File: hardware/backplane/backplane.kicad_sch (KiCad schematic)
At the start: 0 parts

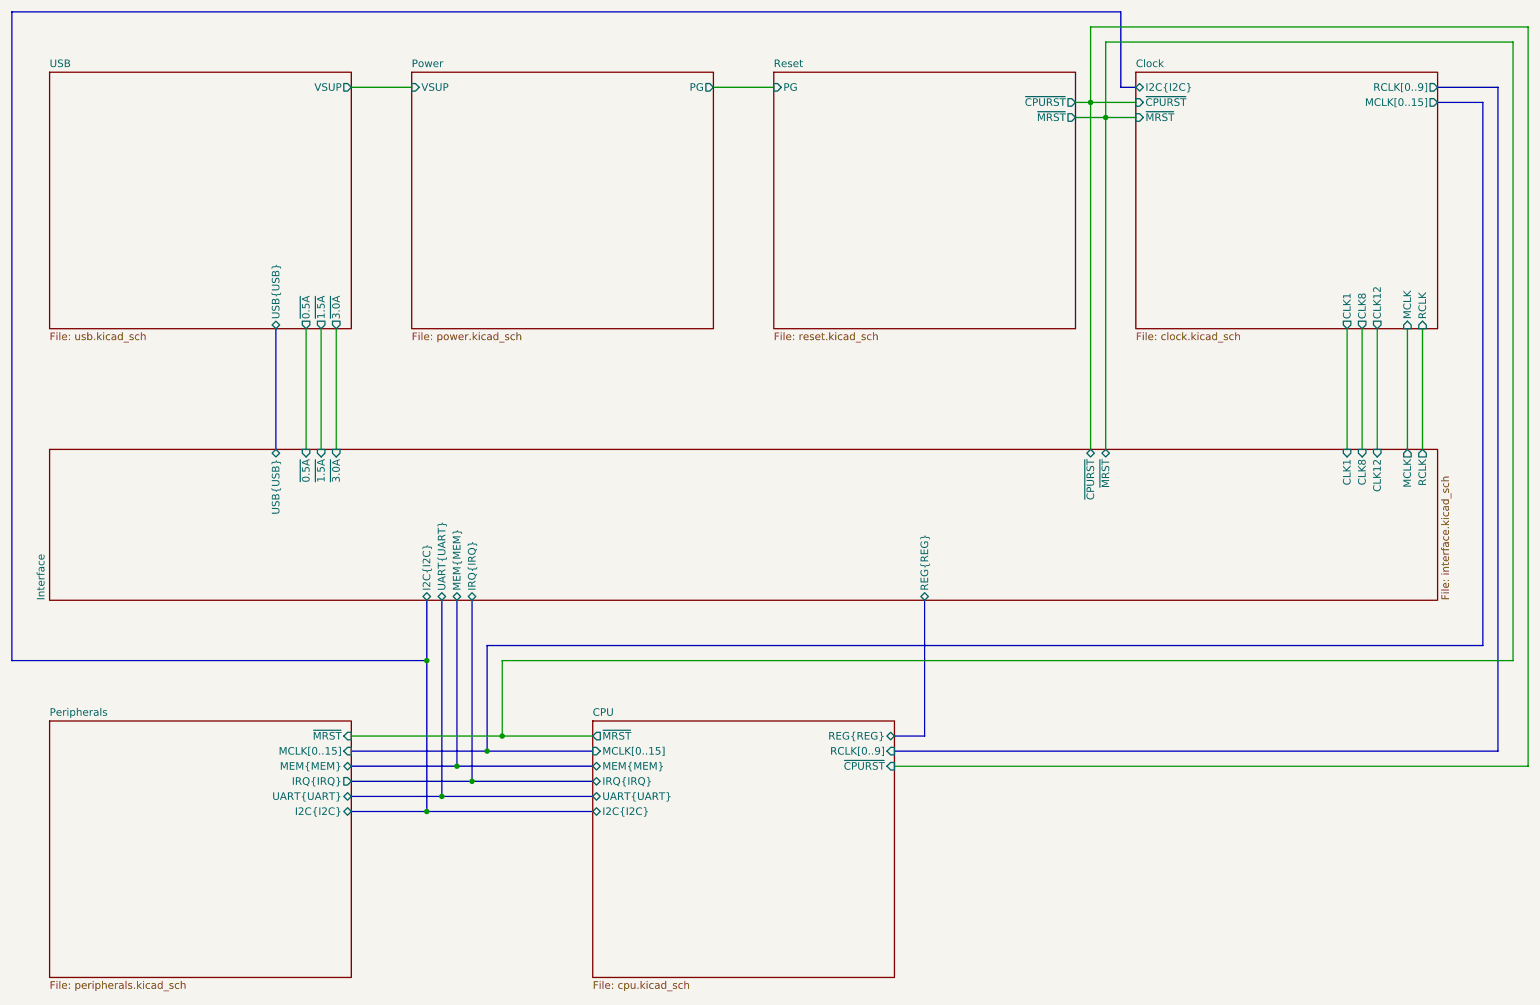
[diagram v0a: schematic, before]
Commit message: feat: Re-add peripheral MCLK, add to memory lines (#3)
Need MCLK to maintain peripheral synchronization.  Add missing memory
access size and latch lines.
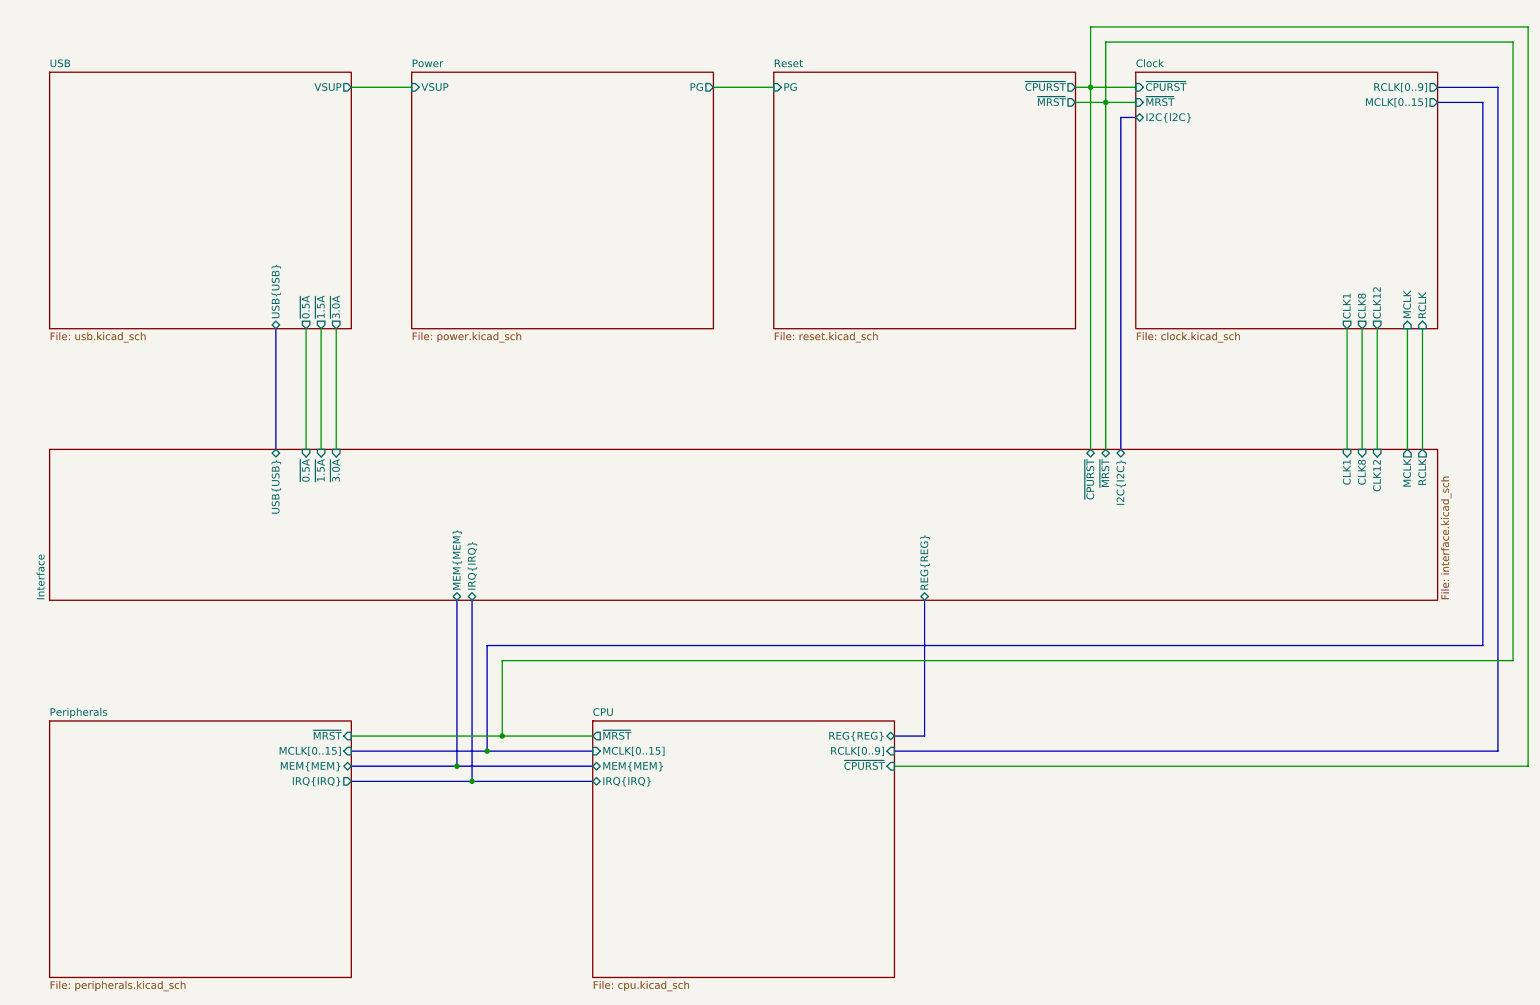
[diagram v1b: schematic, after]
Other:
- sheet CPU ports: added none; removed I2C{I2C}, UART{UART}
- sheet Interface ports: added none; removed UART{UART}
- sheet Peripherals ports: added none; removed I2C{I2C}, UART{UART}

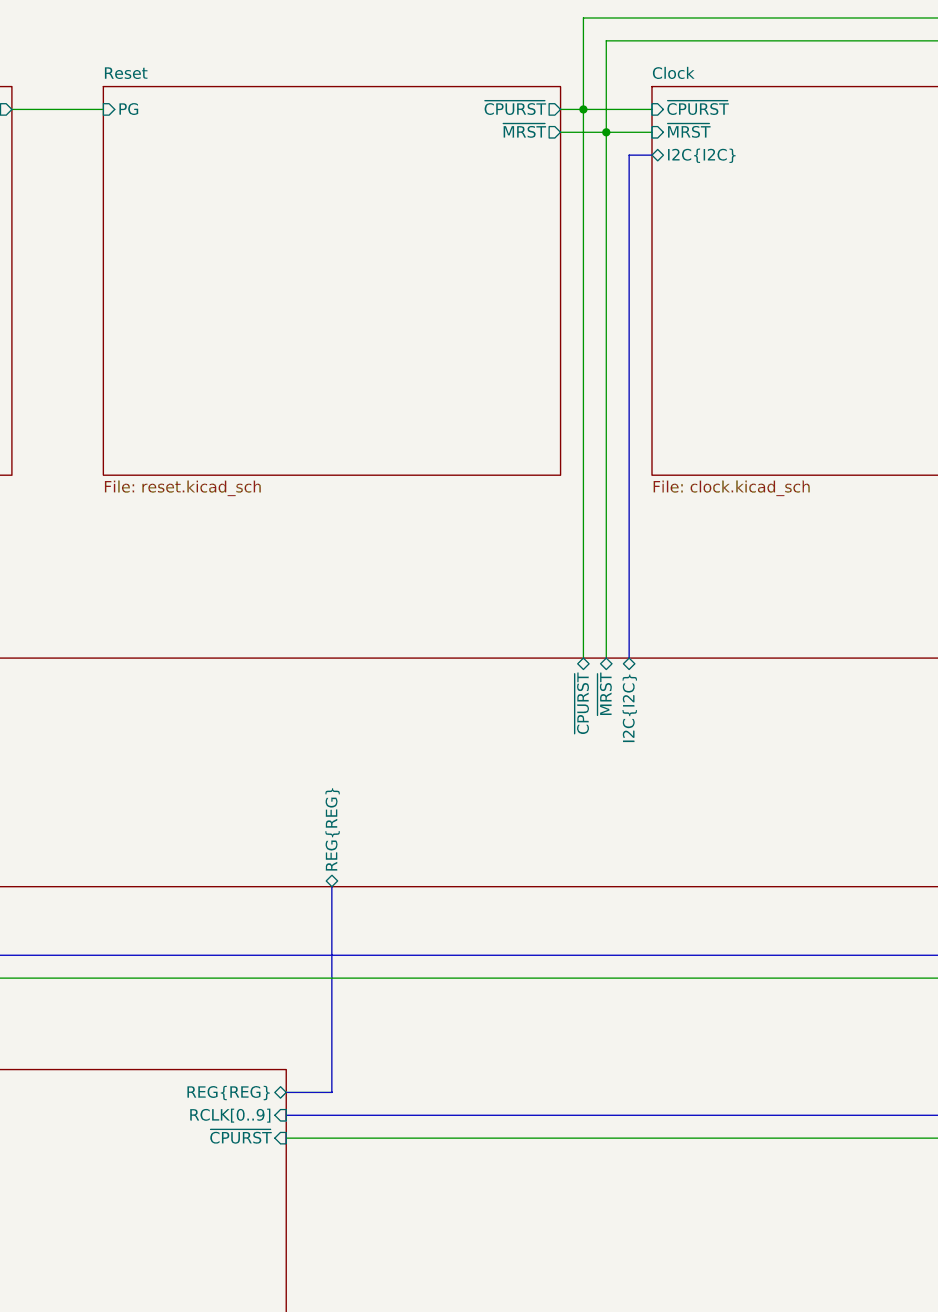
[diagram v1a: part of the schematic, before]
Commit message: feat: Apply bus arch changes to backplane schematic
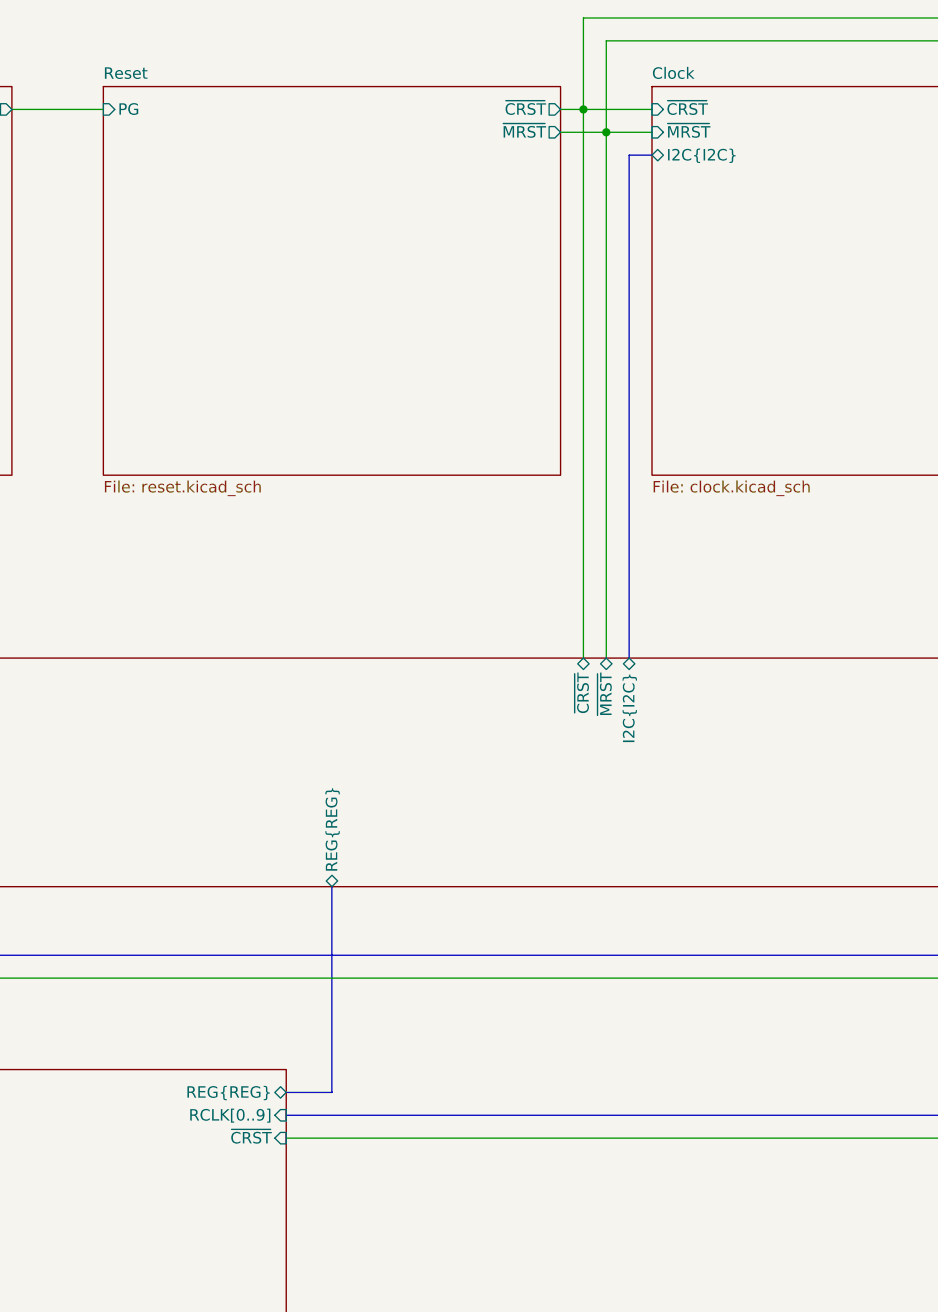
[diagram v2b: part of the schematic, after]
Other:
- sheet CPU ports: added ~{CRST}; removed ~{CPURST}
- sheet Clock ports: added ~{CRST}; removed ~{CPURST}
- sheet Interface ports: added ~{CRST}; removed ~{CPURST}
- sheet Reset ports: added ~{CRST}; removed ~{CPURST}
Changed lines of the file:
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@@
 	)
 	(bus_alias "MEM"
-		(members "A[0..27]" "D[0..31]" "RE" "WE" "HALFWORD" "BYTE" "LATCH")
+		(members "A[0..27]" "D[0..31]" "HALF[0..1]" "~{ARDY}" "~{DRDY}" "~{FAULT}"
+			"~{WR}"
+		)
 	)
 	(bus_alias "REG"
-		(members "SEL[0..11]" "D[0..31]" "DIR")
-	)
-	(bus_alias "SID"
-		(members "[0..3]")
+		(members "R[0..11]" "D[0..31]" "~{WR}")
 	)
 	(bus_alias "UART"
@@
 			)
 		)
-		(pin "~{CPURST}" input
+		(pin "~{CRST}" input
 			(at 165.1 146.05 0)
 			(effects
@@
 			)
 		)
-		(pin "~{CPURST}" bidirectional
+		(pin "~{CRST}" bidirectional
 			(at 198.12 92.71 90)
 			(effects
@@
 			)
 		)
-		(pin "~{CPURST}" input
+		(pin "~{CRST}" input
 			(at 205.74 31.75 180)
 			(effects
@@
 			)
 		)
+		(pin "~{CRST}" output
+			(at 195.58 31.75 0)
+			(effects
+				(font
+					(size 1.27 1.27)
+				)
+				(justify right)
+			)
+		)
 		(pin "~{MRST}" output
 			(at 195.58 34.29 0)
 			(effects
 				(font
-					(size 1.27 1.27)
-				)
-				(justify right)
-			)
-		)
-		(pin "~{CPURST}" output
-			(at 195.58 31.75 0)
-			(effects
-				(font
